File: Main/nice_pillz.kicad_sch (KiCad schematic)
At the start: 22 parts, among them J1 Conn_01x13, J10 BatteryTerminal, J2 Conn_01x13, J3 Conn_01x13, J4 Conn_01x13, J5 Conn_01x10, J6 Conn_01x10, J7 Conn_01x13, J8 Conn_01x13, J9 ChassisButton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

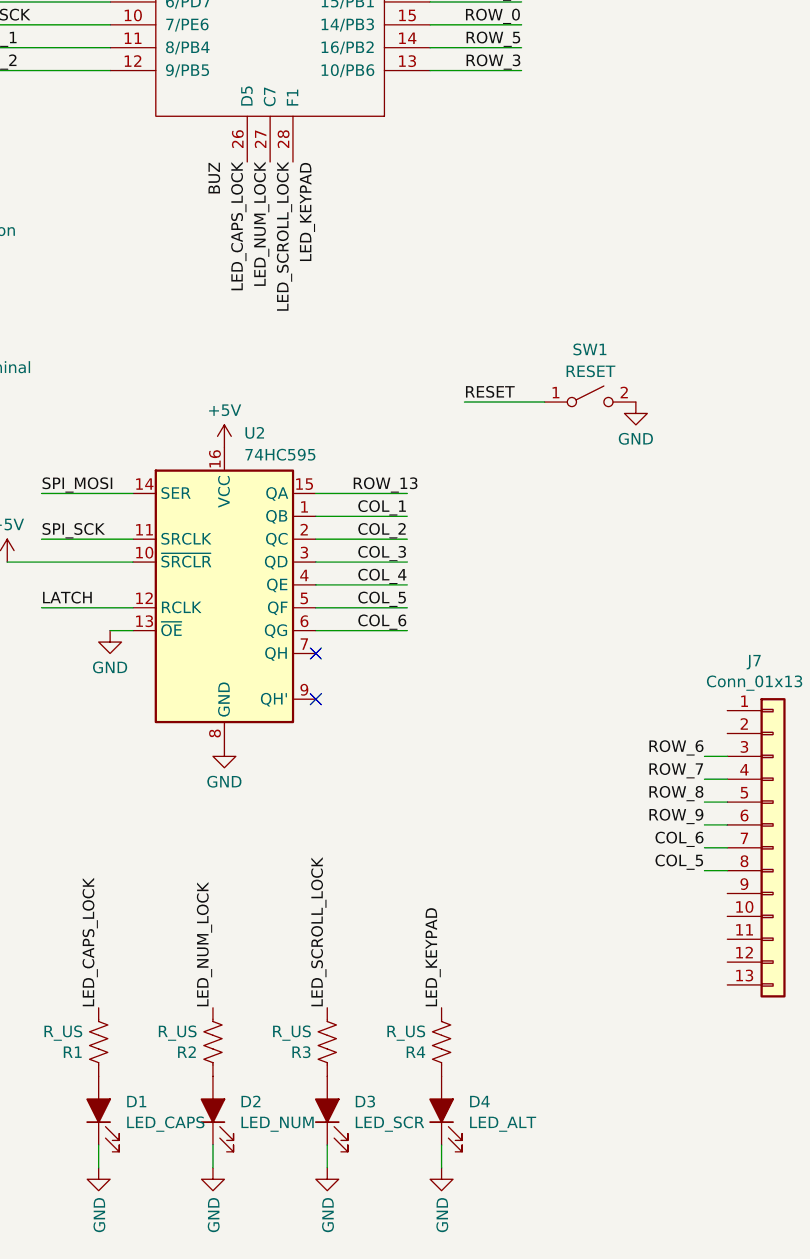
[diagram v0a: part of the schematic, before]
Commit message: v1.1 new pcb and overlay config
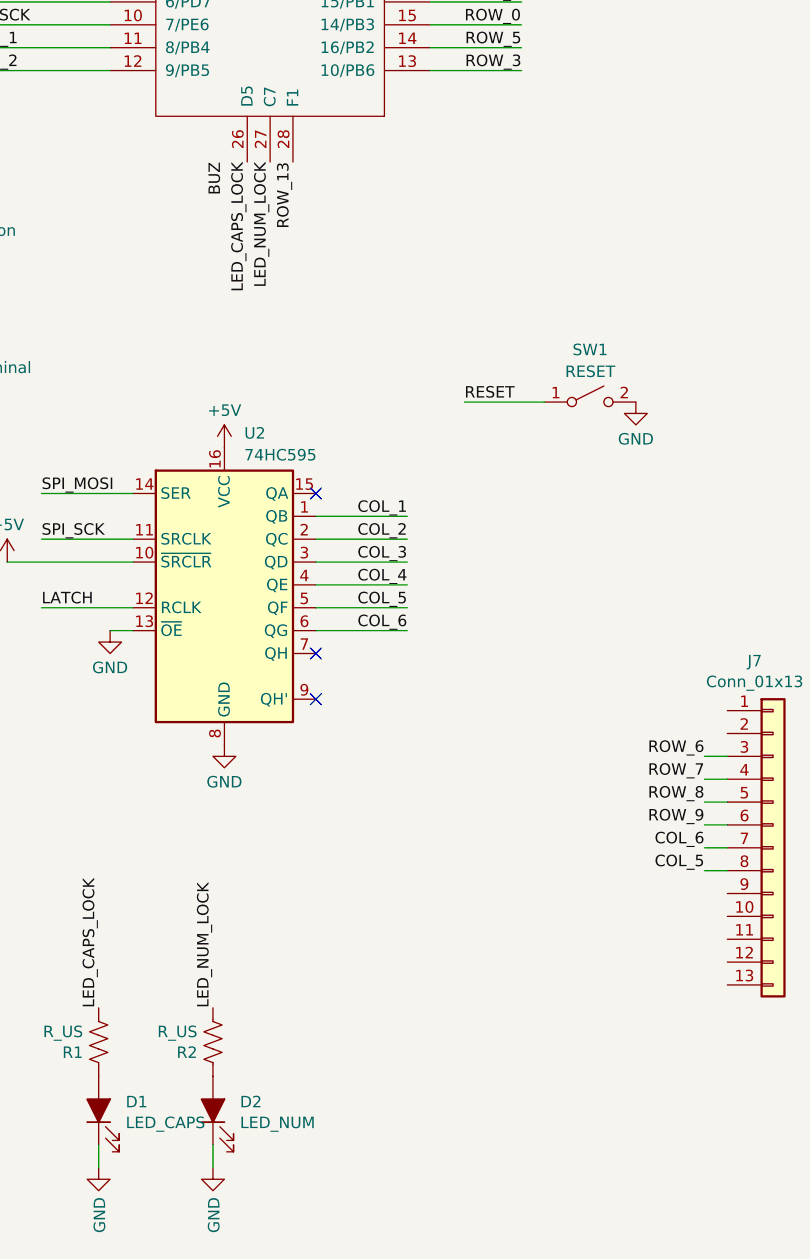
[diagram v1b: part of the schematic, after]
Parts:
- removed D3: LED_SCR, LED_THT:LED_D3.0mm, symbol kicad_port-rescue:LED_ALT-Device
- removed D4: LED_ALT, LED_THT:LED_D3.0mm, symbol kicad_port-rescue:LED_ALT-Device
- removed R3, R4: R_US, Resistor_THT:R_Axial_DIN0204_L3.6mm_D1.6mm_P5.08mm_Horizontal, symbol kicad_port-rescue:R_US-Device
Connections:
- net LED_SCROLL_LOCK is gone; now on net ROW_13: U1.28 (F1)
- no-connect marks 26 -> 27
